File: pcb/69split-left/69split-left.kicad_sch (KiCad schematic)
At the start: 0 parts

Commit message: Figured out what GPIOs to use.
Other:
- note added: "69SPLIT LEFT KEYBOARD"
- note added: "GPIO Outputs"
- note added: "Keyboard USB-C Connection"
- note added: "Right Keyboard"
- note added: "USB-C to PC"
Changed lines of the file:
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@@
 	(generator_version "9.0")
 	(paper "A4")
+	(rectangle
+		(start 167.64 82.55)
+		(end 222.885 140.97)
+		(stroke
+			(width 0)
+			(type solid)
+			(color 0 0 194 1)
+		)
+		(fill
+			(type none)
+		)
+	)
+	(arc
+		(start 120.65 82.55)
+		(mid 158.75 45.1202)
+		(end 196.85 82.55)
+		(stroke
+			(width 0)
+			(type solid)
+			(color 0 0 0 1)
+		)
+		(fill
+			(type none)
+		)
+	)
+	(text "USB-C to PC"
+		(exclude_from_sim no)
+		(at 93.98 57.15 0)
+		(effects
+			(font
+				(size 1.27 1.27)
+				(color 0 0 0 1)
+			)
+			(justify left)
+		)
+	)
+	(text "Keyboard USB-C Connection"
+		(exclude_from_sim no)
+		(at 144.78 52.07 0)
+		(effects
+			(font
+				(size 1.27 1.27)
+				(color 0 0 0 1)
+			)
+			(justify left)
+		)
+	)
+	(text "GPIO Outputs"
+		(exclude_from_sim no)
+		(at 206.375 57.15 0)
+		(effects
+			(font
+				(size 1.27 1.27)
+				(color 0 0 0 1)
+			)
+			(justify left)
+		)
+	)
+	(text "Right Keyboard"
+		(exclude_from_sim no)
+		(at 195.199 111.633 0)
+		(effects
+			(font
+				(size 1.27 1.27)
+			)
+		)
+	)
+	(text "69SPLIT LEFT KEYBOARD"
+		(exclude_from_sim no)
+		(at 137.922 33.02 0)
+		(effects
+			(font
+				(face "Book Antiqua")
+				(size 7.62 7.62)
+				(color 0 0 0 1)
+			)
+		)
+	)
+	(polyline
+		(pts
+			(xy 101.6 59.69) (xy 101.6 82.55)
+		)
+		(stroke
+			(width 0)
+			(type default)
+			(color 0 0 0 1)
+		)
+	)
+	(polyline
+		(pts
+			(xy 212.725 59.436) (xy 212.725 82.296)
+		)
+		(stroke
+			(width 0)
+			(type default)
+			(color 0 0 0 1)
+		)
+	)
+	(polyline
+		(pts
+			(xy 207.645 59.436) (xy 207.645 82.296)
+		)
+		(stroke
+			(width 0)
+			(type default)
+			(color 0 0 0 1)
+		)
+	)
+	(polyline
+		(pts
+			(xy 96.52 59.69) (xy 96.52 82.55)
+		)
+		(stroke
+			(width 0)
+			(type default)
+			(color 0 0 0 1)
+		)
+	)
+	(polyline
+		(pts
+			(xy 217.805 59.436) (xy 217.805 82.296)
+		)
+		(stroke
+			(width 0)
+			(type default)
+			(color 0 0 0 1)
+		)
+	)
 	(sheet
-		(at 124.46 58.42)
+		(at 68.58 82.55)
 		(size 59.69 58.42)
 		(exclude_from_sim no)
@@
 		)
 		(property "Sheetname" "69split Left Keyboard"
-			(at 124.46 57.7084 0)
+			(at 68.58 81.8384 0)
 			(effects
 				(font
@@
 		)
 		(property "Sheetfile" "../left.kicad_sch"
-			(at 124.46 117.4246 0)
+			(at 68.58 141.5546 0)
 			(effects
 				(font

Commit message: Moved things around so it's less confusing.
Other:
- removed sheet 69split Left Keyboard
- added sheet ATmega32U4 (atmega32u4.kicad_sch)
- added sheet Indicator LEDs (indicators.kicad_sch)
- added sheet Left Keyboard Connector (left-conn.kicad_sch)
- added sheet Left Matrix (left-matrix.kicad_sch)
- added sheet USB Connector (usb-conn.kicad_sch)
- note added: "69SPLIT KEYBOARD"
- note added: "LEFT SIDE"
- note removed: "69SPLIT LEFT KEYBOARD"

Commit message: Continued layout.
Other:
- title: (none) -> 69SPLIT KEYBOARD
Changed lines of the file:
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@@
 	(generator_version "9.0")
 	(paper "A4")
+	(title_block
+		(title "69SPLIT KEYBOARD")
+		(date "2025-06-21")
+		(rev "1")
+		(comment 1 "Yiannis Michael")
+		(comment 2 "ymich9963")
+	)
 	(rectangle
 		(start 199.771 75.692)
@@
 	)
 	(embedded_fonts no)
+	(embedded_files
+		(file
+			(name "my-sheet.kicad_wks")
+			(type worksheet)
+			(data |KLUv/WCfCS0VANadXiEQ0zb8P046AJ8aXgsH2O6IQXYrqPActbgvTGkjAgg3cCBVAFEAWAB7LP/L
+				zyw/g9G7Wic1Zntj95csGrCl1TMfak8mtWjA1HoO6fM/+QsAQEBgcj6flV5SJ+kwd6Ip+S7f25nM
+				GINlrZ1uvU6W+ty5UwAEBOfG04UeqDeFmyYieCK/t9h7g3Z+MoMOuug/ORp83WKgi71+31ftVAA8
+				WV6s4+tnaUpW8v/k/x7XCV+vGPTZIKmvv5fN7NVDMu9M7hJ8sfpv709J8jx65IM514baP+fMNtk7
+				OIwGoSb5e+MuL76z6U0o2QSbhPQWiuXnFKVZMkonUyxL8tADtUPyJ/M4lqCllL0iEm2jZJZugSk0
+				h4iAKab4XrVeFOEITC/EKOOwRZdVtgGB4bqUou7OZ4UirF9WRavlIhkEIlGAPic93r72wtU1YXvp
+				pShb6XVcXYu6cFVVWjU4bMJlWWOzrIlSECySPTSGZoBa9F674fqtaLXZg9M48TV3bYCCoOFA5pgZ
+				GklBmgxjgESExqwbzSlGCpJs4MLuYpN32QM4R7fcqQEYZYbBFb1roCZzALF1NlkveCyCWL35cxnE
+				wEKI4KJj0KsXBr6oiI1J+MtQQe+wUhcnvps4Rq/BHcNqTNlOEzNBhptObKt4AIWcYgJSlH9RNGOF
+				4k2HgwPJg0yfmc/CAzU75BLHuyCsTniNFbERpgVEeEgINsEyhIZBhCUXYQhCwScM5iHza+yObgD2
+				rqfvQX3GtNTki66yMw857Cm3qOsujTSVhoEY/SH9Q5Ui707wgLy7+D2sP38Sbw3rjn/tfXLTei5t
+				wgDnVU9KDVYzrAHGAIE4CQf8nZQ1Aw8ByJ0t3qRoW1pWI4TomR9hr1HcpCVt2Lj0DctF1FRG+kCN
+				Qa8C|
+			)
+			(checksum "4C3981DD706FE33EF3AD57A4258970D5")
+		)
+	)
 )

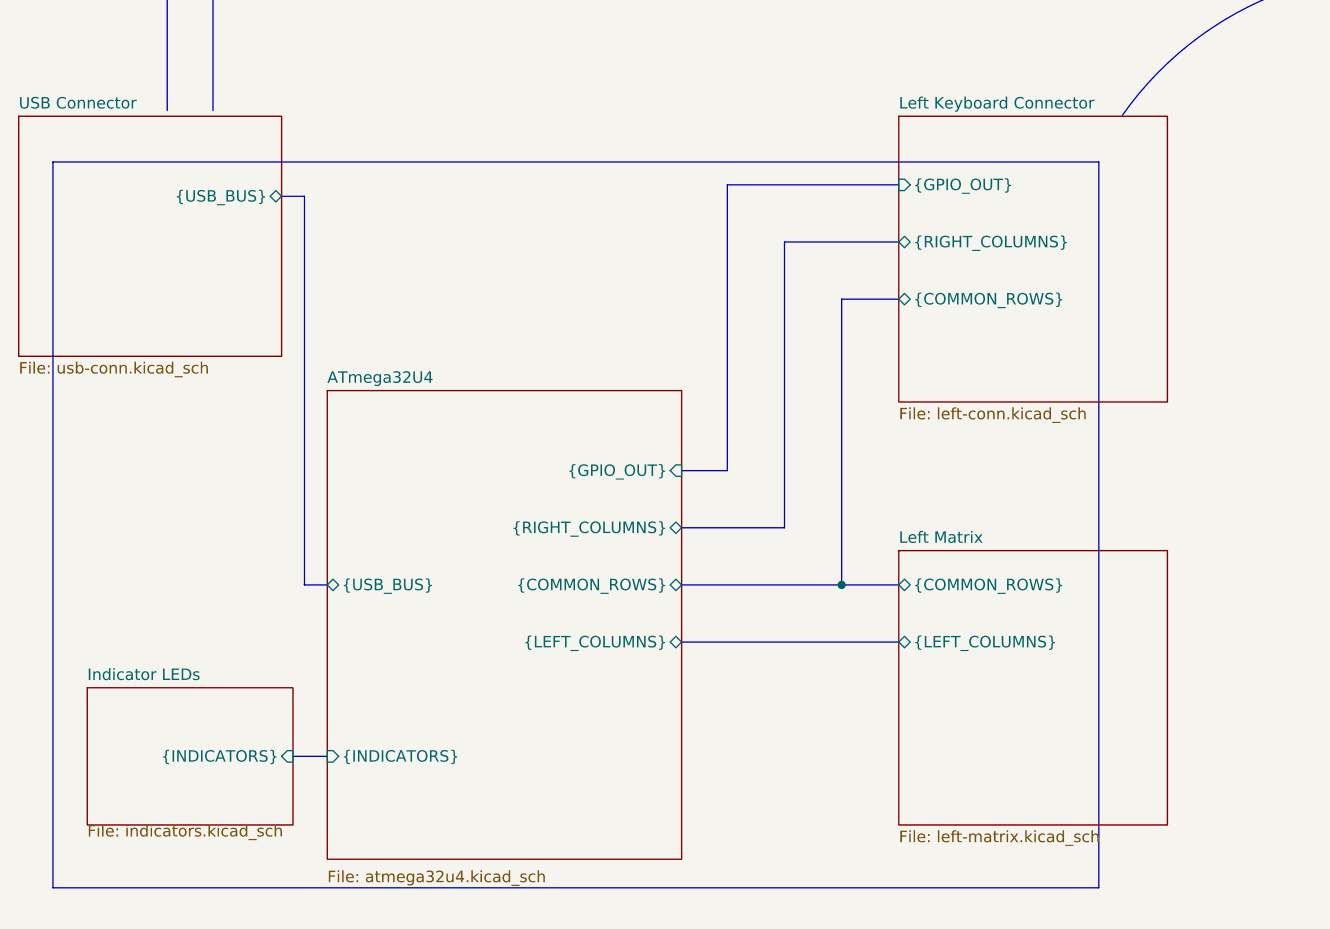
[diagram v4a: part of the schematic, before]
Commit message: Practically finished the left side - need to make a footprint for the split USB connector. Some other schematic changes were made that I will not list. I should've made more commits between ths one and the previous one but it is what it is.
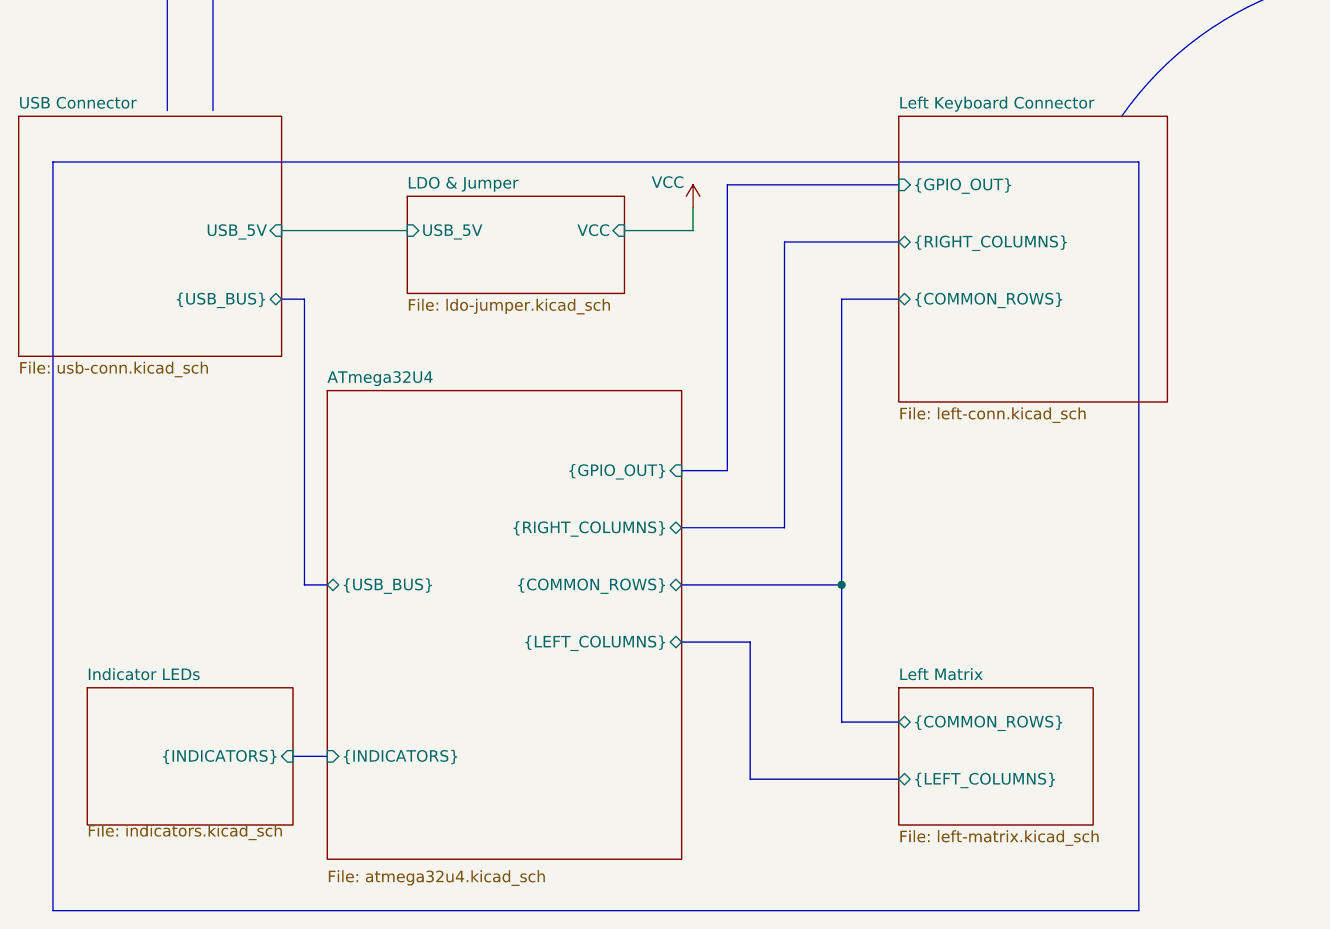
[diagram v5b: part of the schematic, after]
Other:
- added sheet LDO & Jumper (ldo-jumper.kicad_sch)
- sheet USB Connector ports: added USB_5V; removed none
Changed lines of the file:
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@@
 	(rectangle
 		(start 48.26 81.28)
-		(end 164.465 161.925)
+		(end 168.91 164.465)
 		(stroke
 			(width 0)
@@
 	(bus
 		(pts
-			(xy 76.2 85.09) (xy 76.2 128.27)
+			(xy 76.2 96.52) (xy 76.2 128.27)
 		)
 		(stroke
@@
 	(bus
 		(pts
-			(xy 135.89 128.27) (xy 142.24 128.27)
+			(xy 135.89 143.51) (xy 142.24 143.51)
 		)
 		(stroke
@@
 	(bus
 		(pts
+			(xy 125.73 134.62) (xy 118.11 134.62)
+		)
+		(stroke
+			(width 0)
+			(type default)
+		)
+	)
+	(bus
+		(pts
 			(xy 123.19 83.82) (xy 142.24 83.82)
 		)
@@
 		)
 	)
-	(bus
-		(pts
-			(xy 118.11 134.62) (xy 142.24 134.62)
+	(wire
+		(pts
+			(xy 119.38 88.9) (xy 119.38 86.36)
+		)
+		(stroke
+			(width 0)
+			(type default)
+		)
+	)
+	(bus
+		(pts
+			(xy 125.73 149.86) (xy 142.24 149.86)
+		)
+		(stroke
+			(width 0)
+			(type default)
+		)
+	)
+	(bus
+		(pts
+			(xy 135.89 143.51) (xy 135.89 128.27)
 		)
 		(stroke
@@
 	(bus
 		(pts
-			(xy 73.66 85.09) (xy 76.2 85.09)
+			(xy 73.66 96.52) (xy 76.2 96.52)
+		)
+		(stroke
+			(width 0)
+			(type default)
+		)
+	)
+	(bus
+		(pts
+			(xy 125.73 149.86) (xy 125.73 134.62)
+		)
+		(stroke
+			(width 0)
+			(type default)
+		)
+	)
+	(wire
+		(pts
+			(xy 111.76 88.9) (xy 119.38 88.9)
+		)
+		(stroke
+			(width 0)
+			(type default)
+		)
+	)
+	(wire
+		(pts
+			(xy 73.66 88.9) (xy 87.63 88.9)
 		)
 		(stroke
@@
 			(type default)
 			(color 0 0 0 1)
+		)
+	)
+	(symbol
+		(lib_id "power:VCC")
+		(at 119.38 86.36 0)
+		(unit 1)
+		(exclude_from_sim no)
+		(in_bom yes)
+		(on_board yes)
+		(dnp no)
+		(property "Reference" "#PWR018"
+			(at 119.38 90.17 0)
+			(effects
+				(font
+					(size 1.27 1.27)
+				)
+				(hide yes)
+			)
+		)
+		(property "Value" "VCC"
+			(at 116.586 83.566 0)
+			(effects
+				(font
+					(size 1.27 1.27)
+				)
+			)
+		)
+		(property "Footprint" ""
+			(at 119.38 86.36 0)
+			(effects
+				(font
+					(size 1.27 1.27)
+				)
+				(hide yes)
+			)
+		)
+		(property "Datasheet" ""
+			(at 119.38 86.36 0)
+			(effects
+				(font
+					(size 1.27 1.27)
+				)
+				(hide yes)
+			)
+		)
+		(property "Description" ""
+			(at 119.38 86.36 0)
+			(effects
+				(font
+					(size 1.27 1.27)
+				)
+			)
+		)
+		(pin "1"
+		)
+		(instances
+			(project "69split-left"
+				(path "/94301c1c-44b1-4926-ac38-8a25b84a2b23"
+					(reference "#PWR018")
+					(unit 1)
+				)
+			)
 		)
 	)
@@
 	)
 	(sheet
-		(at 142.24 124.46)
-		(size 29.845 30.48)
+		(at 142.24 139.7)
+		(size 21.59 15.24)
 		(exclude_from_sim no)
 		(in_bom yes)
@@
 		)
 		(property "Sheetname" "Left Matrix"
-			(at 142.24 123.7484 0)
+			(at 142.24 138.9884 0)
 			(effects
 				(font
@@
 		)
 		(pin "{COMMON_ROWS}" bidirectional
-			(at 142.24 128.27 180)
+			(at 142.24 143.51 180)
 			(effects
 				(font
@@
 		)
 		(pin "{LEFT_COLUMNS}" bidirectional
-			(at 142.24 134.62 180)
+			(at 142.24 149.86 180)
 			(effects
 				(font
@@
 		)
 		(pin "{USB_BUS}" bidirectional
-			(at 73.66 85.09 0)
+			(at 73.66 96.52 0)
+			(effects
+				(font
+					(size 1.27 1.27)
+				)
+				(justify right)
+			)
+		)
+		(pin "USB_5V" input
+			(at 73.66 88.9 0)
 			(effects
 				(font
@@
 				)
 			)
+		)
+	)
+	(sheet
+		(at 87.63 85.09)
+		(size 24.13 10.795)
+		(exclude_from_sim no)
+		(in_bom yes)
+		(on_board yes)
+		(dnp no)
+		(fields_autoplaced yes)
+		(stroke
+			(width 0.1524)
+			(type solid)
+		)
+		(fill
+			(color 0 0 0 0.0000)
+		)
+		(property "Sheetname" "LDO & Jumper"
+			(at 87.63 84.3784 0)
+			(effects
+				(font
+					(size 1.27 1.27)
+				)
+				(justify left bottom)
+			)
+		)
+		(property "Sheetfile" "ldo-jumper.kicad_sch"
+			(at 87.63 96.4696 0)
+			(effects
+				(font
+					(size 1.27 1.27)
+				)
+				(justify left top)
+			)
+		)
+		(pin "USB_5V" input
+			(at 87.63 88.9 180)
+			(effects
+				(font
+					(size 1.27 1.27)
+				)
+				(justify left)
+			)
+		)
+		(pin "VCC" input
+			(at 111.76 88.9 0)
+			(effects
+				(font
+					(size 1.27 1.27)
+				)
+				(justify right)
+			)
+		)
+		(instances
+			(project "69split-left"
+				(path "/94301c1c-44b1-4926-ac38-8a25b84a2b23"
+					(page "7")
+				)
+			)

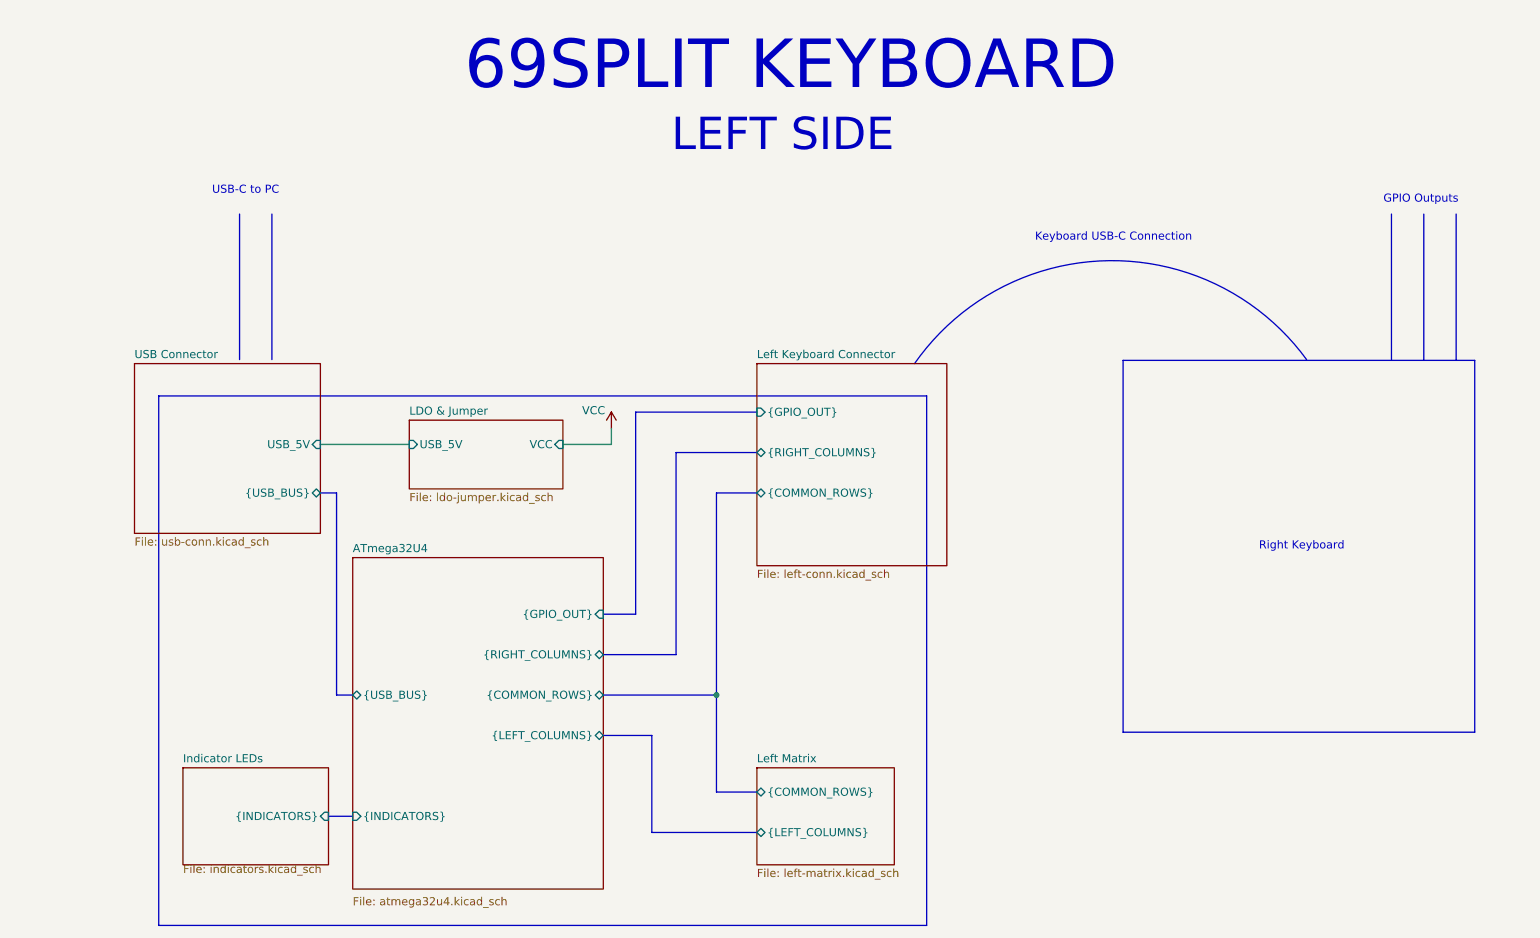
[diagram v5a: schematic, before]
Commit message: Started changing things gain to use an I/O expander with I2C.
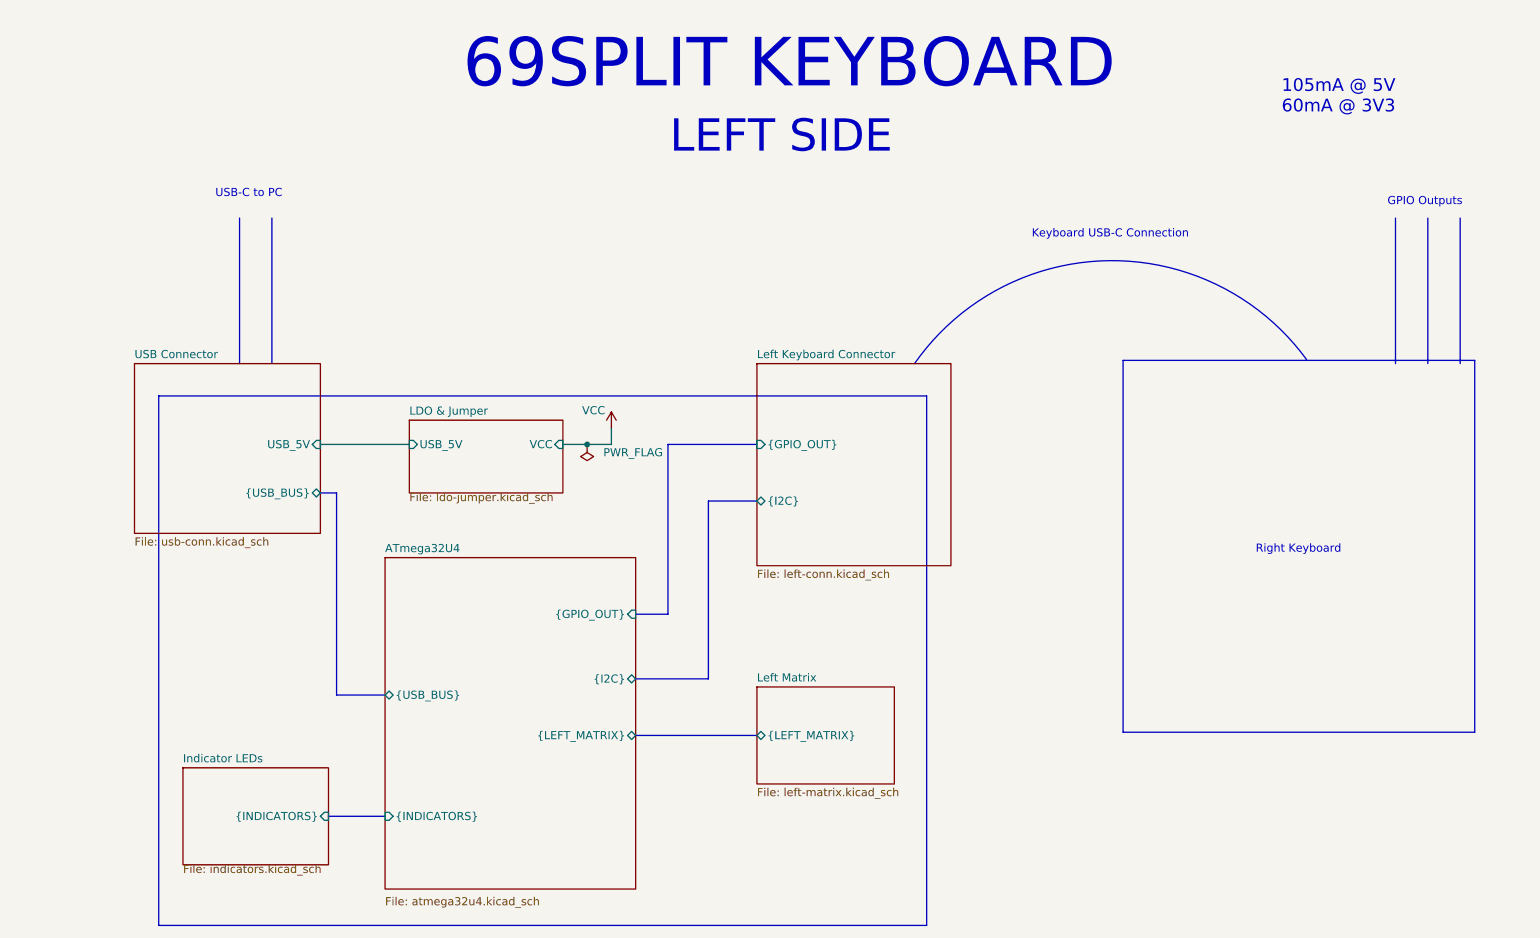
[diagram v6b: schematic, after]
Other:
- sheet ATmega32U4 ports: added {I2C}, {LEFT_MATRIX}; removed {COMMON_ROWS}, {LEFT_COLUMNS}, {RIGHT_COLUMNS}
- sheet Left Keyboard Connector ports: added {I2C}; removed {COMMON_ROWS}, {RIGHT_COLUMNS}
- sheet Left Matrix ports: added {LEFT_MATRIX}; removed {COMMON_ROWS}, {LEFT_COLUMNS}
- note added: "105mA @ 5V 60mA @ 3V3"
- company: (none) -> Yiannis Michael
- title: 69SPLIT KEYBOARD -> 69SPLIT

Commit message: Finished left keyboard again...
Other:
- added sheet Breakout Header (breakout-header.kicad_sch)
- sheet ATmega32U4 ports: added {BREAKOUT_HEADER}; removed none
- sheet LDO & Jumper ports: added 3V3; removed none

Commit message: I think the right side is done???. Added image and 3D files.
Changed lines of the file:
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@@
 		(on_board yes)
 		(dnp no)
-		(fields_autoplaced yes)
 		(stroke
 			(width 0.1524)
@@
 		)
 		(property "Sheetfile" "left-conn.kicad_sch"
-			(at 142.24 108.5346 0)
+			(at 142.24 109.728 0)
 			(effects
 				(font
